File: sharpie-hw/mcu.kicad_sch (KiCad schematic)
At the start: 37 parts, among them J3 Conn_01x03_MountingPin, J4 Conn_01x08, SW1 SW_Push_Cross, SW2 SW_Push_Cross, U3 RP2350_60QFN, U4 W25Q128JVS, Y1 Crystal_GND24

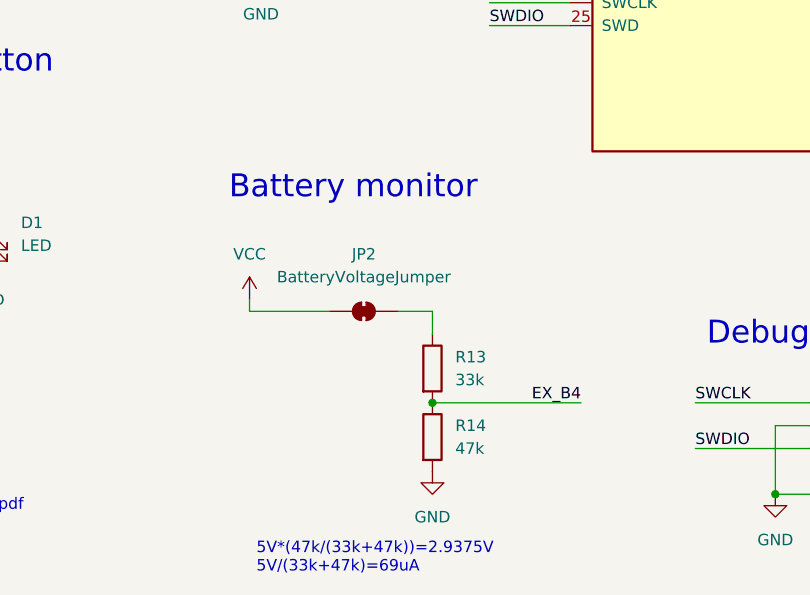
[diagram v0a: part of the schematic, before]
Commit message: PCB changes of some kind: appears to be the version sent to JLC.
The manufactured version of the PCB has no voltage divider or battery input,
because they were unnecssary (and in the case of the battery input,
unsafe).
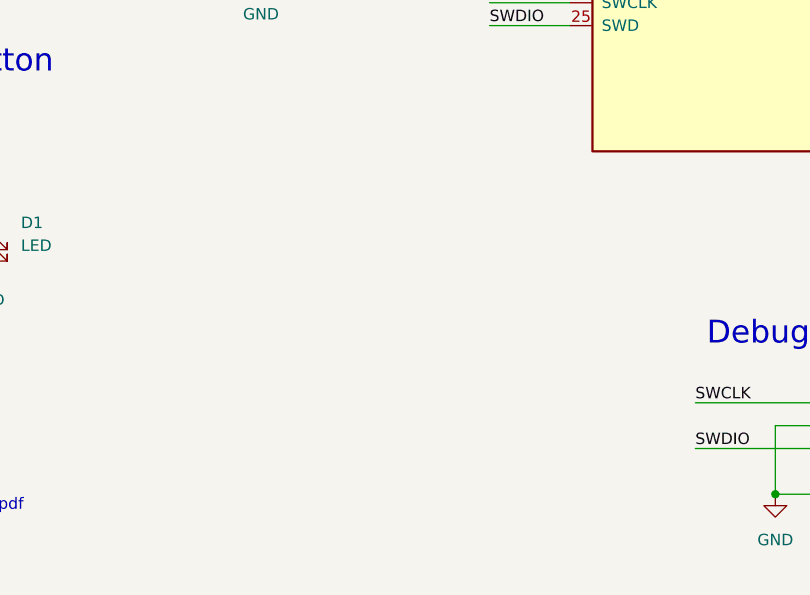
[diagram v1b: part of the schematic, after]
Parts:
- removed JP2: BatteryVoltageJumper, Jumper:SolderJumper-2_P1.3mm_Bridged_Pad1.0x1.5mm, symbol Jumper:SolderJumper_2_Bridged
- removed R13: 33k, Resistor_SMD:R_0402_1005Metric, symbol Device:R
- removed R14: 47k, Resistor_SMD:R_0402_1005Metric, symbol Device:R
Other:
- note removed: "5V*(47k/(33k+47k))=2.9375V 5V/(33k+47k)=69uA"
- note removed: "Battery monitor"
